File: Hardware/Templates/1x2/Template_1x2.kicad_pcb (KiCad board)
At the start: 2 copper layers, 42 x 84 mm, 4 parts

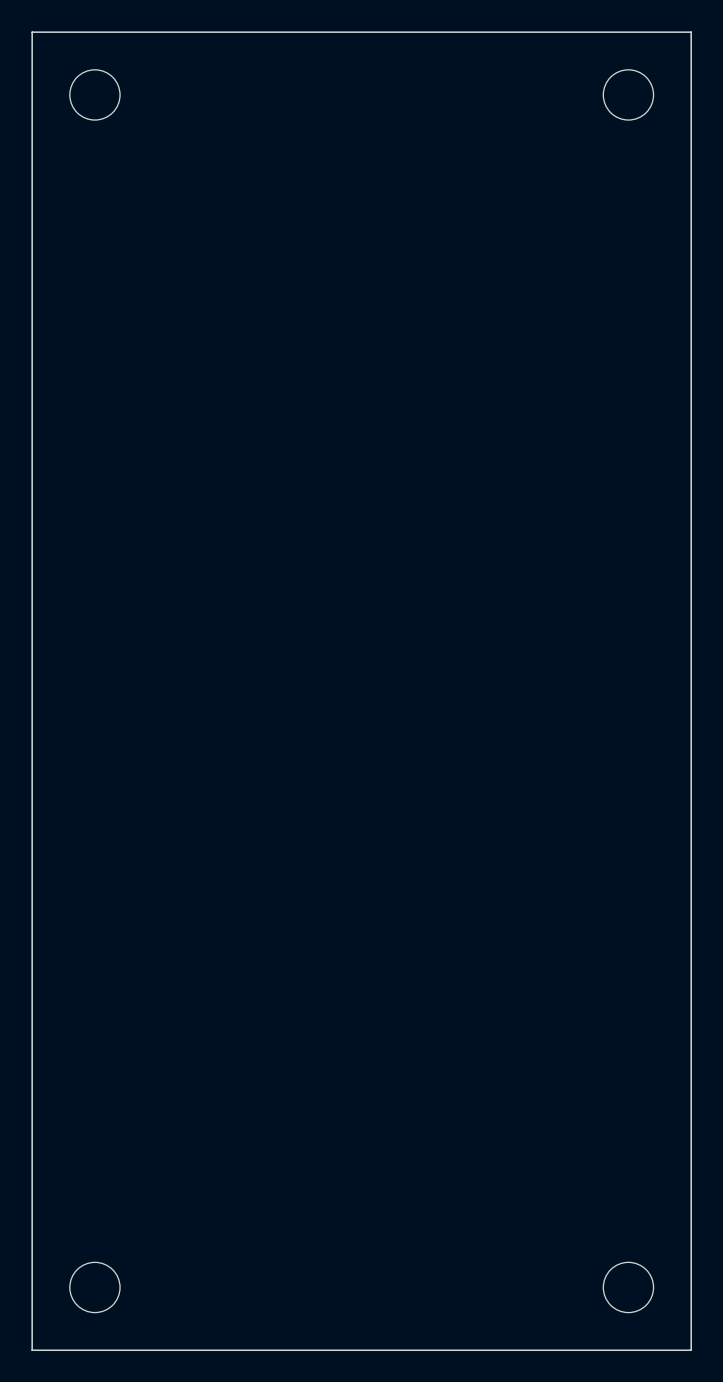
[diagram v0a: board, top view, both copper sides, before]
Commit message: Edited Templates for Hardware
Edited size of templates to fit within containers
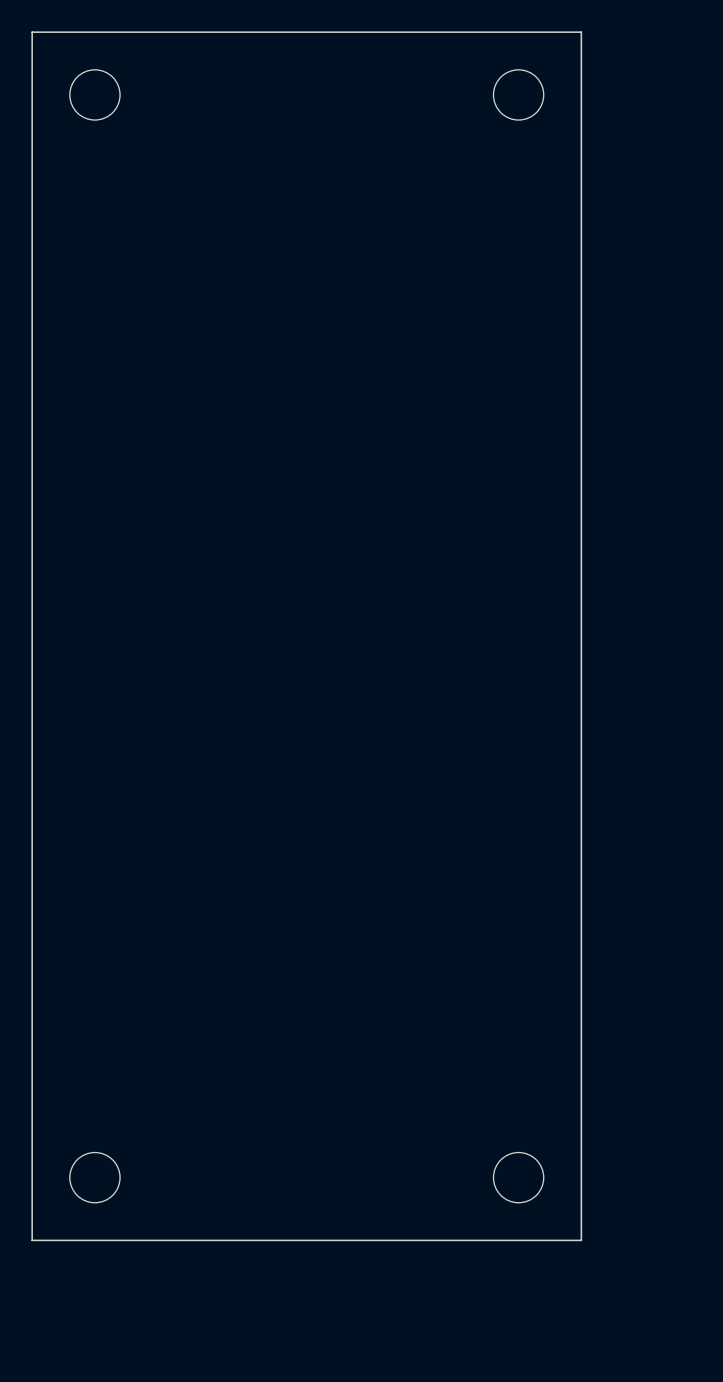
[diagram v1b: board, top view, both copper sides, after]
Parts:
- moved REF** 9.90 mm to (51.0, 93.0)
- moved REF** 7.00 mm to (51.0, 24.0)
- moved REF** 7.00 mm to (24.0, 93.0)
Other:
- board size 42 x 84 mm -> 35 x 77 mm
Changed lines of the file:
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@@
 	(footprint "MountingHole:MountingHole_3.2mm_M3"
 		(layer "F.Cu")
-		(at 58 100)
+		(at 51 93)
 		(descr "Mounting Hole 3.2mm, no annular, M3")
 		(tags "mounting hole 3.2mm no annular m3")
@@
 	(footprint "MountingHole:MountingHole_3.2mm_M3"
 		(layer "F.Cu")
-		(at 58 24)
+		(at 51 24)
 		(descr "Mounting Hole 3.2mm, no annular, M3")
 		(tags "mounting hole 3.2mm no annular m3")
@@
 	(footprint "MountingHole:MountingHole_3.2mm_M3"
 		(layer "F.Cu")
-		(at 24 100)
+		(at 24 93)
 		(descr "Mounting Hole 3.2mm, no annular, M3")
 		(tags "mounting hole 3.2mm no annular m3")
@@
 	(gr_rect
 		(start 20 20)
-		(end 62 104)
+		(end 55 97)
 		(stroke
 			(width 0.1)
